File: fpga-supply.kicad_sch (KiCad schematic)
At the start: 180 parts, among them J19 15910060, J20 15910060, U1 XC7K410T-2FFG900I

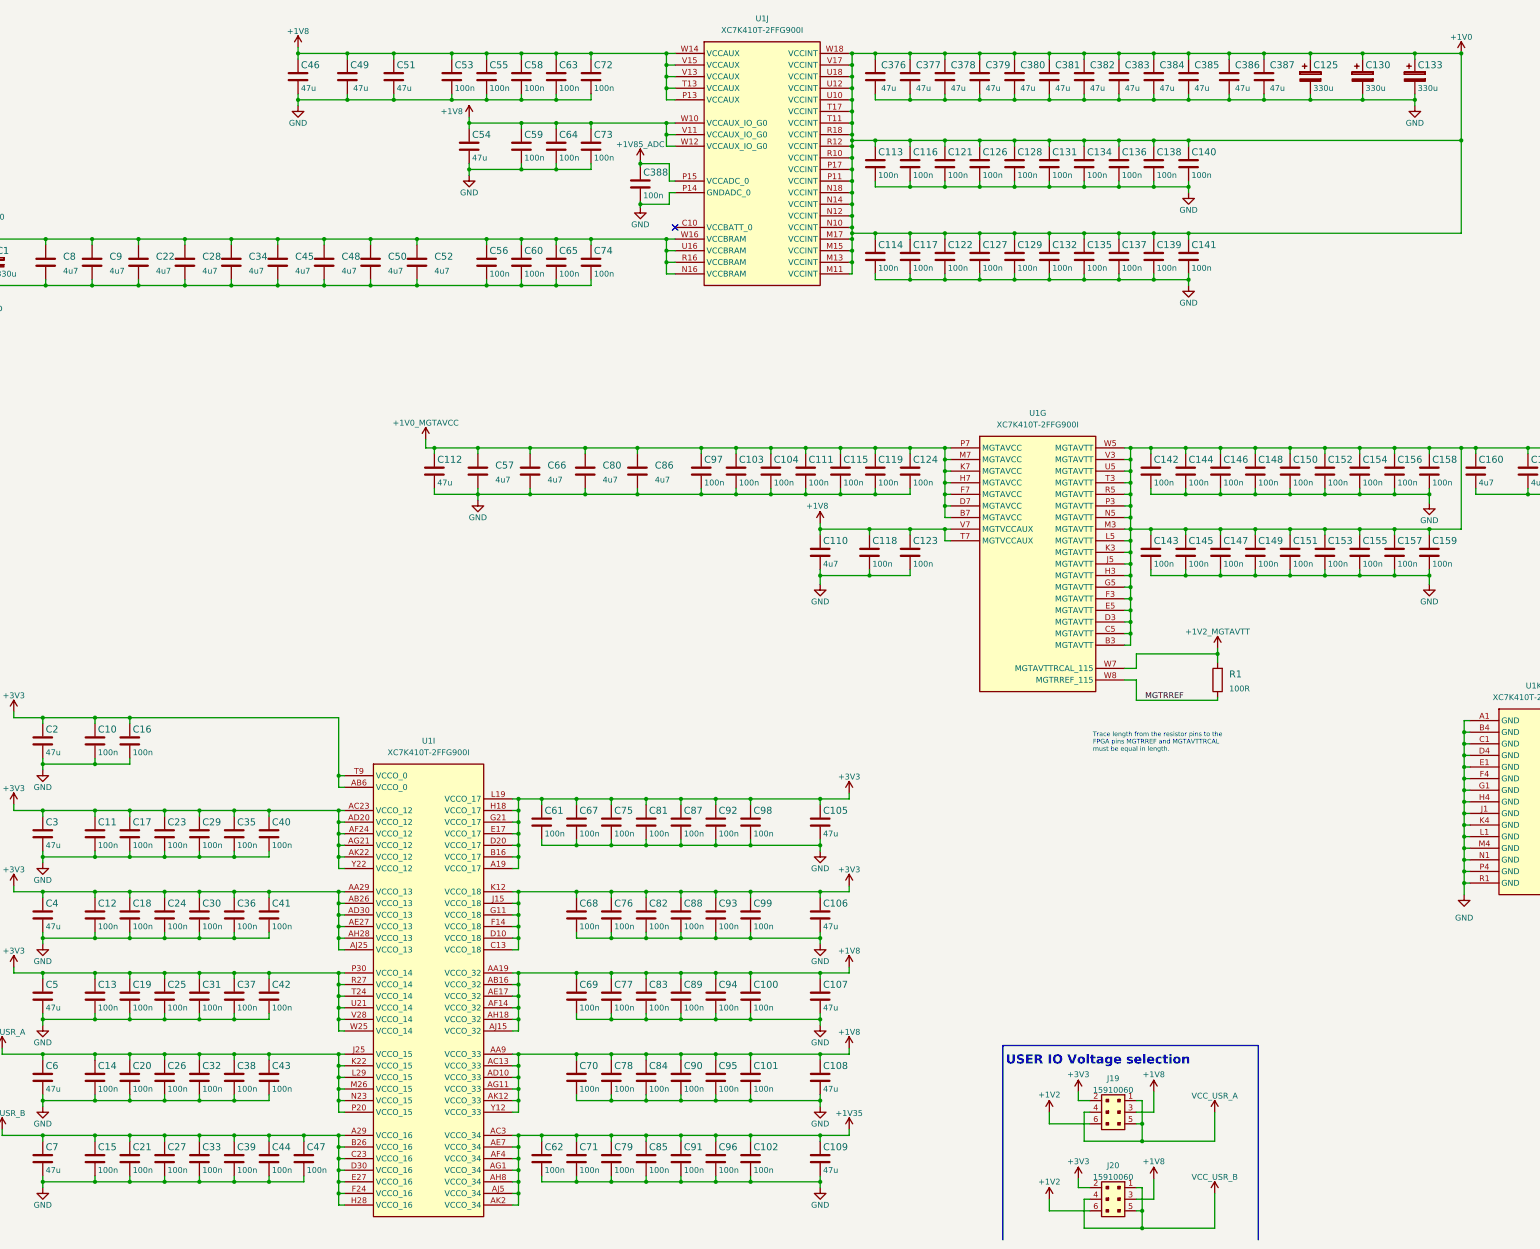
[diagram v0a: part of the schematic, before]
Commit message: Replace 100n to 0402
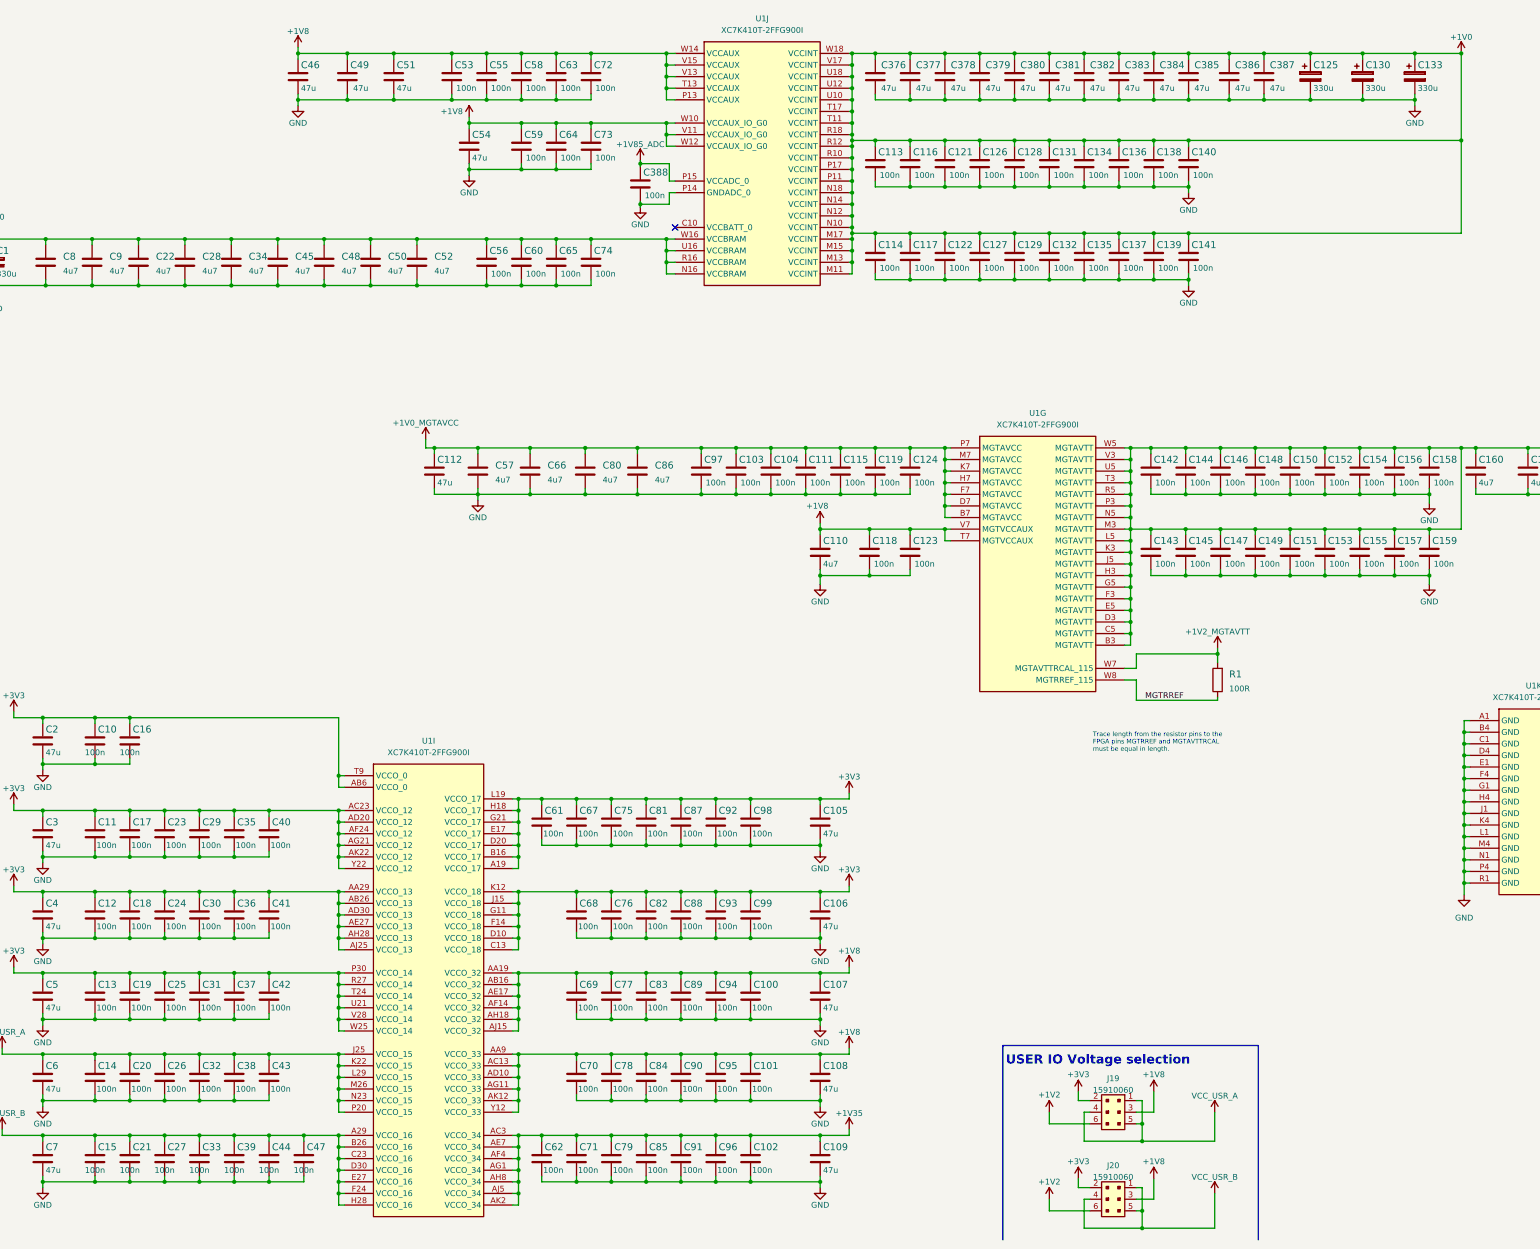
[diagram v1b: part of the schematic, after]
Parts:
- C10, C100, C101, C102, C103, C104, C11, C111, C113, C114, C115, C116, C117, C118, C119, C12, C121, C122, C123, C124, C126, C127, C128, C129, C13, C131, C132, C134, C135, C136, C137, C138, C139, C14, C140, C141, C142, C143, C144, C145, C146, C147, C148, C149, C15, C150, C151, C152, C153, C154, C155, C156, C157, C158, C159, C16, C17, C18, C19, C20, C21, C23, C24, C25, C26, C27, C29, C30, C31, C32, C33, C35, C36, C37, C38, C388, C39, C40, C41, C42, C43, C44, C47, C53, C55, C56, C58, C59, C60, C61, C62, C63, C64, C65, C67, C68, C69, C70, C71, C72, C73, C74, C75, C76, C77, C78, C79, C81, C82, C83, C84, C85, C87, C88, C89, C90, C91, C92, C93, C94, C95, C96, C97, C98, C99: value C_100n_0201 -> C_100n_0402_EIA; footprint antmicro-footprints:0201-res -> antmicro-footprints:0402-cap_EIA; symbol antmicroCapacitorsmisc:C_100n_0201 -> antmicroCapacitors0402:C_100n_0402_EIA; MPN CC0201KRX6S5BB104 -> GRM155R61H104KE14D; Manufacturer YAGEO -> Murata

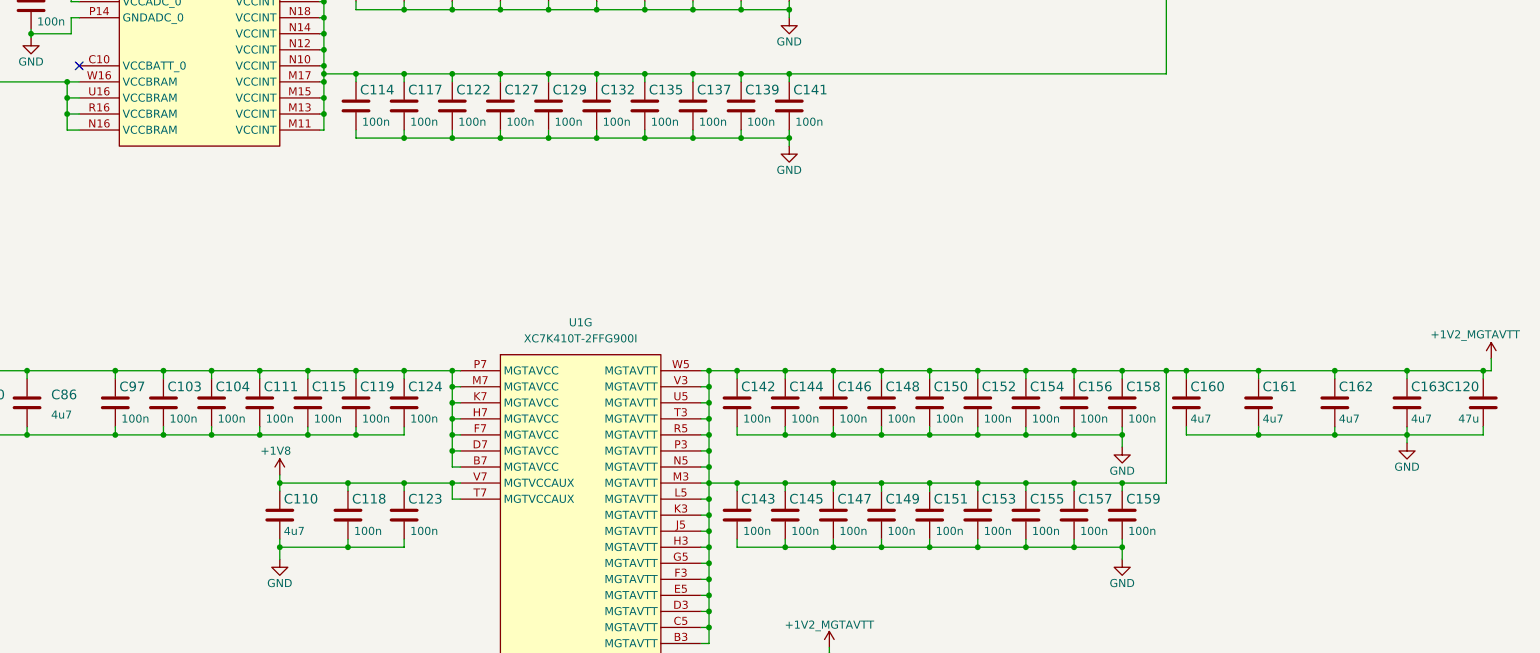
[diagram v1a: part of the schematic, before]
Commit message: Increase 0201 to 0402 components where possible (EIA 0402 footprint)
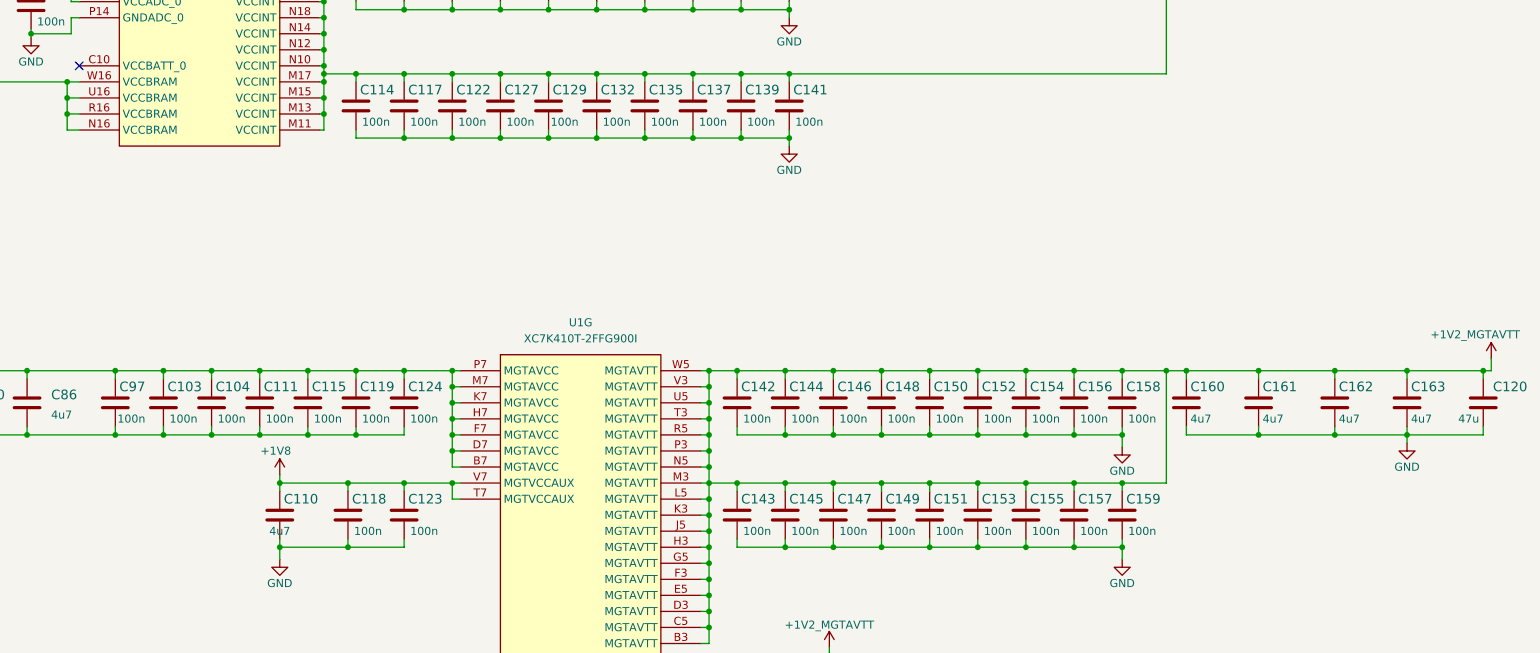
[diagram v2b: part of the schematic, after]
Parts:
- C104, C115, C122, C124, C126, C127, C129, C132, C135, C137, C139, C141, C142, C144, C145, C146, C147, C148, C149, C150, C151, C152, C153, C154, C156, C157, C158, C159, C388, C56, C60, C65, C74, C97: value C_100n_0402_EIA -> C_100n_0201; footprint antmicro-footprints:0402-cap_EIA -> antmicro-footprints:0201-cap; symbol antmicroCapacitors0402:C_100n_0402_EIA -> antmicroCapacitorsmisc:C_100n_0201; MPN GRM155R61H104KE14D -> CC0201KRX6S5BB104; Manufacturer Murata -> YAGEO
- C110: value C_4u7_0402 -> C_4u7_0402_EIA; footprint antmicro-footprints:0402-cap -> antmicro-footprints:0201-cap; symbol antmicroCapacitors0402:C_4u7_0402 -> antmicroCapacitorsmisc:C_4u7_0201; MPN GRM155R61A475MEAAD -> GRM035R60J475ME15D; Manufacturer MURATA -> Murata
- C160, C161, C162, C163, C22, C28, C34, C45, C48, C50, C52, C57, C66, C8, C80, C86, C9: footprint antmicro-footprints:0201-res -> antmicro-footprints:0201-cap

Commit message: Update signage
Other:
- moved on the sheet: C1, C10, C100, C101, C102, C103, C104, C105, C106, C107, C108, C109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

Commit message: Loclib
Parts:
- C1, C125, C130, C133: footprint antmicro-footprints:KEMET_B -> K410T-devboard-footprints:KEMET_B; symbol antmicroCapacitorspol:C_330u_KEMET_B -> K410T-devboard:C_330u_KEMET_B
- C10, C100, C101, C102, C103, C11, C111, C113, C114, C116, C117, C118, C119, C12, C121, C123, C128, C13, C131, C134, C136, C138, C14, C140, C143, C15, C155, C16, C17, C18, C19, C20, C21, C23, C24, C25, C26, C27, C29, C30, C31, C32, C33, C35, C36, C37, C38, C39, C40, C41, C42, C43, C44, C47, C53, C55, C58, C59, C61, C62, C63, C64, C67, C68, C69, C70, C71, C72, C73, C75, C76, C77, C78, C79, C81, C82, C83, C84, C85, C87, C88, C89, C90, C91, C92, C93, C94, C95, C96, C98, C99: footprint antmicro-footprints:0402-cap_EIA -> K410T-devboard-footprints:0402-cap_EIA; symbol antmicroCapacitors0402:C_100n_0402_EIA -> K410T-devboard:C_100n_0402_EIA
- C104, C115, C122, C124, C126, C127, C129, C132, C135, C137, C139, C141, C142, C144, C145, C146, C147, C148, C149, C150, C151, C152, C153, C154, C156, C157, C158, C159, C388, C56, C60, C65, C74, C97: footprint antmicro-footprints:0201-cap -> K410T-devboard-footprints:0201-cap; symbol antmicroCapacitorsmisc:C_100n_0201 -> K410T-devboard:C_100n_0201
- C105, C106, C107, C108, C109, C112, C120, C2, C3, C376, C377, C378, C379, C380, C381, C382, C383, C384, C385, C386, C387, C4, C46, C49, C5, C51, C54, C6, C7: footprint antmicro-footprints:0603-cap -> K410T-devboard-footprints:0603-cap; symbol antmicroCapacitors0603:C_47u_0603 -> K410T-devboard:C_47u_0603
- C110, C160, C161, C162, C163, C22, C28, C34, C45, C48, C50, C52, C57, C66, C8, C80, C86, C9: footprint antmicro-footprints:0201-cap -> K410T-devboard-footprints:0201-cap; symbol antmicroCapacitorsmisc:C_4u7_0201 -> K410T-devboard:C_4u7_0201
- J19, J20: footprint antmicro-footprints:15910060 -> K410T-devboard-footprints:15910060; symbol antmicroRectangularConnectorsHeadersMalePins:15910060 -> K410T-devboard:15910060
- R1: footprint antmicro-footprints:0201-res -> K410T-devboard-footprints:0201-res; symbol antmicroResistorsmisc:R_100R_0201 -> K410T-devboard:R_100R_0201
- U1: footprint antmicro-footprints:xc7k410t-2ffg900I -> K410T-devboard-footprints:xc7k410t-2ffg900I; symbol antmicroMicrocontrollers:XC7K410T-2FFG900I -> K410T-devboard:XC7K410T-2FFG900I
